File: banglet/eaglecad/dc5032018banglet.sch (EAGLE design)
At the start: 40 parts, among them Q3 DMG3415U-7, U2 AP2112(3.3V), U3 MCP73831T-2ACI/OT, U4 CP2104, X1 32.768, X2 JSTPH, X4 20329

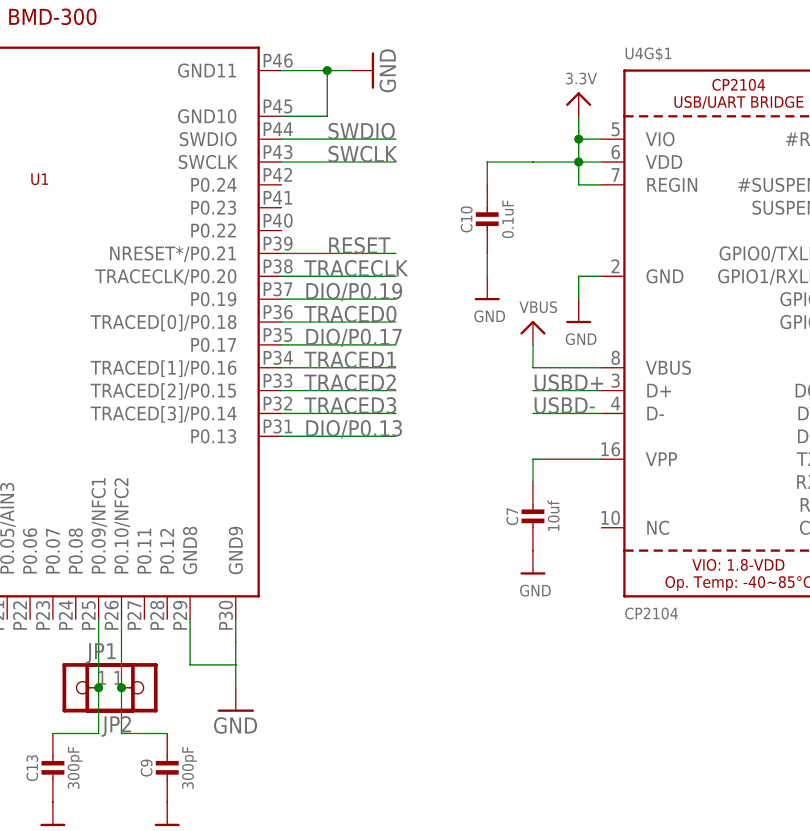
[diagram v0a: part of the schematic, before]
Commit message: Connect the unconnected; add in a junction
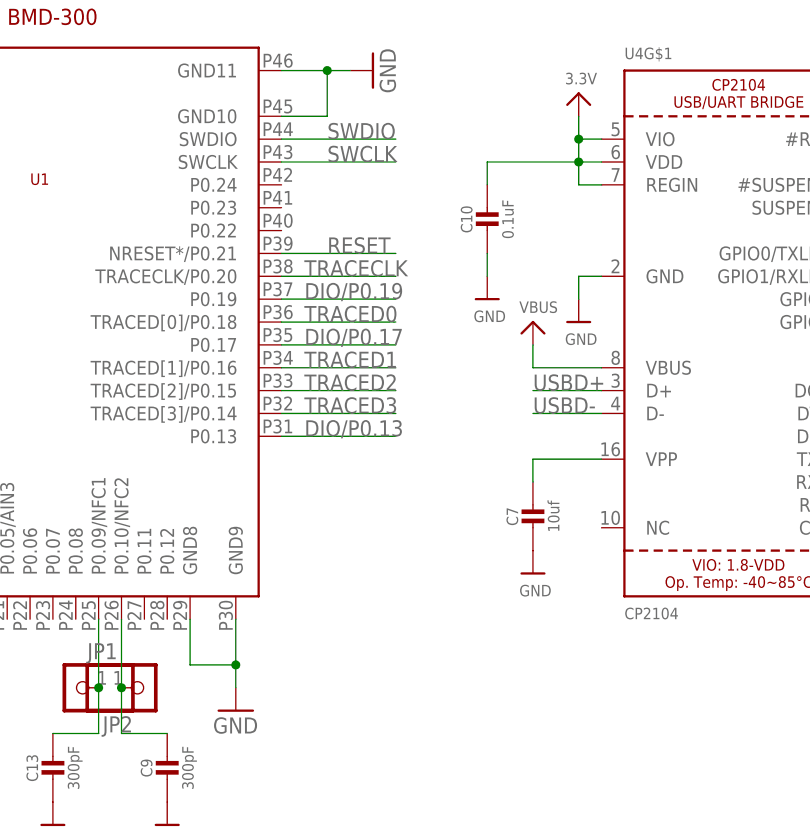
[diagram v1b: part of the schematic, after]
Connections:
- new net DIO/P0.17: U1.P0.17
- new net TRACED0: U1.TRACED[0]/P0.18
- new net TRACED1: U1.TRACED[1]/P0.16
- new net TRACED2: U1.TRACED[2]/P0.15
- new net TRACED3: U1.TRACED[3]/P0.14
- net RESET: now also U1.NRESET*/P0.21
- net SWCLK: now also U1.SWCLK
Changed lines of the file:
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@@
 <?xml version="1.0" encoding="utf-8"?>
 <!DOCTYPE eagle SYSTEM "eagle.dtd">
-<eagle version="8.2.1">
+<eagle version="8.6.3">
 <drawing>
 <settings>
 <setting alwaysvectorfont="no"/>
+<setting keepoldvectorfont="yes"/>
 <setting verticaltext="up"/>
 </settings>
@@
 <wire x1="22.86" y1="-43.18" x2="22.86" y2="-40.64" width="0.1524" layer="91"/>
 <pinref part="U1" gate="G$1" pin="GND8"/>
-<wire x1="22.86" y1="-38.1" x2="22.86" y2="-35.56" width="0.1524" layer="91"/>
 <wire x1="17.78" y1="-35.56" x2="17.78" y2="-40.64" width="0.1524" layer="91"/>
 <wire x1="17.78" y1="-40.64" x2="22.86" y2="-40.64" width="0.1524" layer="91"/>
-<wire x1="22.86" y1="-40.64" x2="22.86" y2="-38.1" width="0.1524" layer="91"/>
+<wire x1="22.86" y1="-40.64" x2="22.86" y2="-35.56" width="0.1524" layer="91"/>
+<junction x="22.86" y="-40.64"/>
 </segment>
 <segment>
@@
 <pinref part="C10" gate="G$1" pin="1"/>
 <wire x1="63.5" y1="15.24" x2="60.96" y2="15.24" width="0.1524" layer="91"/>
-<wire x1="60.96" y1="15.24" x2="55.88" y2="15.24" width="0.1524" layer="91"/>
-<wire x1="55.88" y1="15.24" x2="50.8" y2="15.24" width="0.1524" layer="91"/>
+<wire x1="60.96" y1="15.24" x2="50.8" y2="15.24" width="0.1524" layer="91"/>
 <wire x1="50.8" y1="15.24" x2="50.8" y2="12.7" width="0.1524" layer="91"/>
 <wire x1="60.96" y1="12.7" x2="60.96" y2="15.24" width="0.1524" layer="91"/>
@@
 <wire x1="27.94" y1="5.08" x2="40.64" y2="5.08" width="0.1524" layer="91"/>
 <label x="33.02" y="5.08" size="1.778" layer="95"/>
+<pinref part="U1" gate="G$1" pin="NRESET*/P0.21"/>
 </segment>
 </net>
@@
 <wire x1="27.94" y1="15.24" x2="40.64" y2="15.24" width="0.1524" layer="91"/>
 <label x="33.02" y="15.24" size="1.778" layer="95"/>
+<pinref part="U1" gate="G$1" pin="SWCLK"/>
 </segment>
 </net>
@@
 <wire x1="27.94" y1="-2.54" x2="40.64" y2="-2.54" width="0.1524" layer="91"/>
 <label x="30.48" y="-2.54" size="1.778" layer="95"/>
+<pinref part="U1" gate="G$1" pin="TRACED[0]/P0.18"/>
 </segment>
 </net>
@@
 <wire x1="27.94" y1="-12.7" x2="40.64" y2="-12.7" width="0.1524" layer="91"/>
 <label x="30.48" y="-12.7" size="1.778" layer="95"/>
+<pinref part="U1" gate="G$1" pin="TRACED[3]/P0.14"/>
 </segment>
 </net>
@@
 <wire x1="27.94" y1="-10.16" x2="40.64" y2="-10.16" width="0.1524" layer="91"/>
 <label x="30.48" y="-10.16" size="1.778" layer="95"/>
+<pinref part="U1" gate="G$1" pin="TRACED[2]/P0.15"/>
 </segment>
 </net>
@@
 <wire x1="27.94" y1="-7.62" x2="40.64" y2="-7.62" width="0.1524" layer="91"/>
 <label x="30.48" y="-7.62" size="1.778" layer="95"/>
+<pinref part="U1" gate="G$1" pin="TRACED[1]/P0.16"/>
 </segment>
 </net>
@@
 <wire x1="27.94" y1="-5.08" x2="40.64" y2="-5.08" width="0.1524" layer="91"/>
 <label x="30.48" y="-5.08" size="1.778" layer="95"/>
+<pinref part="U1" gate="G$1" pin="P0.17"/>
 </segment>
 </net>
@@
 </note>
 <note version="8.2" severity="warning">
-Since Version 8.2, Eagle supports online libraries. The ids
+Since Version 8.2, EAGLE supports online libraries. The ids
 of those online libraries will not be understood (or retained)
 with this version.

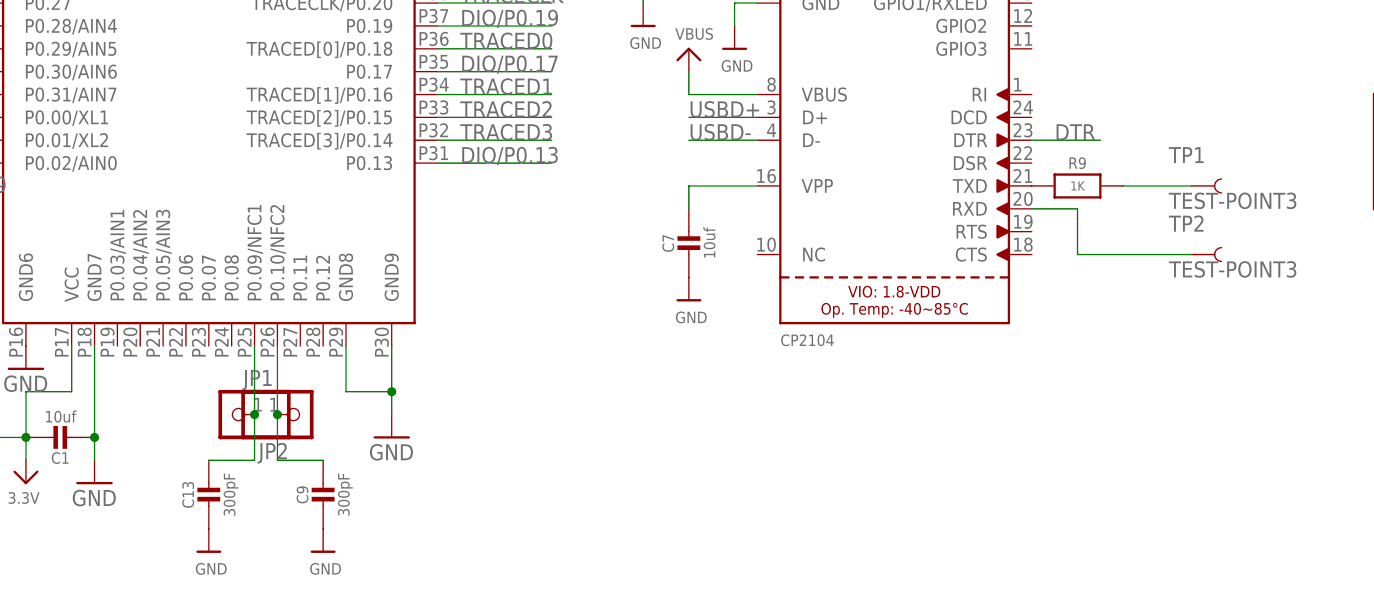
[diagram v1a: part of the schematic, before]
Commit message: connect uart tx/rx to bmd-300
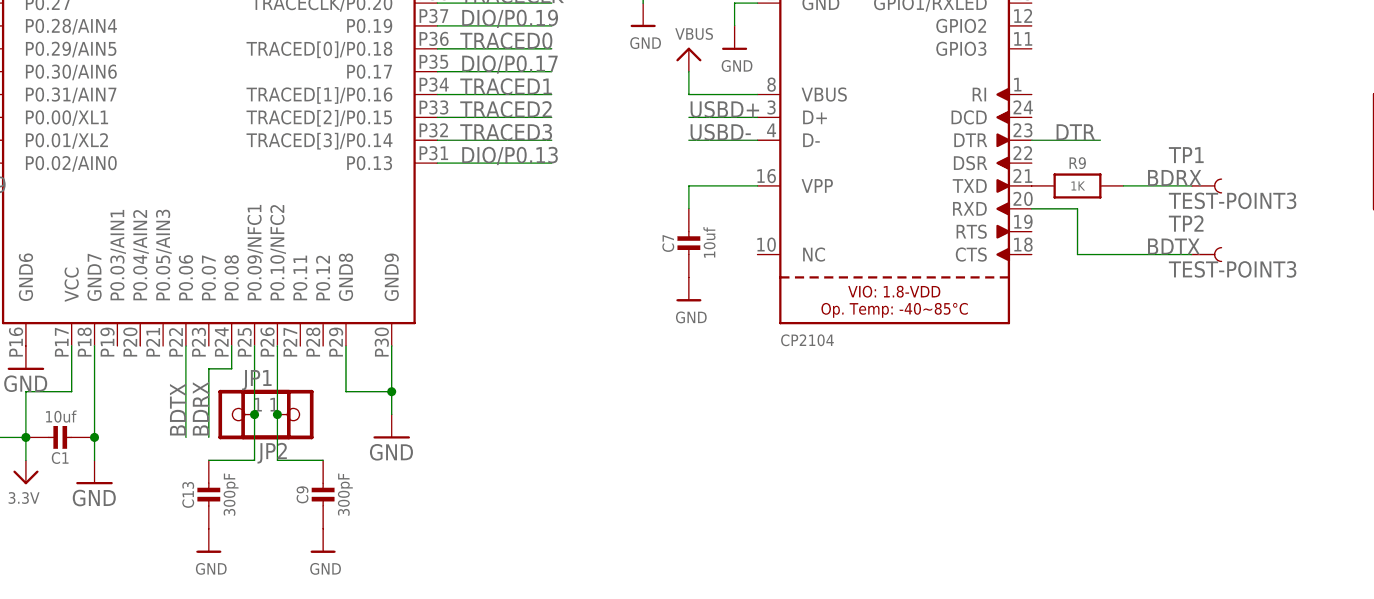
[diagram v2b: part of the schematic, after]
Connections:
- removed net N$3: R9.2, TP1.1
- removed net N$5: TP2.1, U4G$1.RXD
- new net BDRX: R9.2, TP1.1, U1.P0.08
- new net BDTX: TP2.1, U1.P0.06, U4G$1.RXD
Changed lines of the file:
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@@
 </segment>
 </net>
-<net name="VIN" class="0">
+<net name="VIN" class="1">
 <segment>
 <pinref part="D5" gate="G$1" pin="C"/>
@@
 </segment>
 </net>
-<net name="N$3" class="0">
-<segment>
-<pinref part="R9" gate="G$1" pin="2"/>
-<wire x1="111.76" y1="-17.78" x2="104.14" y2="-17.78" width="0.1524" layer="91"/>
-<pinref part="TP1" gate="G$1" pin="1"/>
-</segment>
-</net>
-<net name="N$5" class="0">
-<segment>
-<pinref part="U4" gate="G$1" pin="RXD"/>
-<wire x1="93.98" y1="-20.32" x2="99.06" y2="-20.32" width="0.1524" layer="91"/>
-<wire x1="99.06" y1="-20.32" x2="99.06" y2="-25.4" width="0.1524" layer="91"/>
-<wire x1="99.06" y1="-25.4" x2="111.76" y2="-25.4" width="0.1524" layer="91"/>
-<pinref part="TP2" gate="G$1" pin="1"/>
-</segment>
-</net>
 <net name="N$6" class="0">
 <segment>
@@
 </segment>
 </net>
+<net name="BDRX" class="0">
+<segment>
+<pinref part="U1" gate="G$1" pin="P0.08"/>
+<wire x1="5.08" y1="-35.56" x2="5.08" y2="-38.1" width="0.1524" layer="91"/>
+<wire x1="5.08" y1="-38.1" x2="2.54" y2="-38.1" width="0.1524" layer="91"/>
+<wire x1="2.54" y1="-38.1" x2="2.54" y2="-45.72" width="0.1524" layer="91"/>
+<label x="2.54" y="-45.72" size="1.778" layer="95" rot="R90"/>
+</segment>
+<segment>
+<pinref part="R9" gate="G$1" pin="2"/>
+<wire x1="111.76" y1="-17.78" x2="104.14" y2="-17.78" width="0.1524" layer="91"/>
+<pinref part="TP1" gate="G$1" pin="1"/>
+<label x="106.68" y="-17.78" size="1.778" layer="95"/>
+</segment>
+</net>
+<net name="BDTX" class="0">
+<segment>
+<pinref part="U1" gate="G$1" pin="P0.06"/>
+<wire x1="0" y1="-35.56" x2="0" y2="-45.72" width="0.1524" layer="91"/>
+<label x="0" y="-45.72" size="1.778" layer="95" rot="R90"/>
+</segment>
+<segment>
+<pinref part="U4" gate="G$1" pin="RXD"/>
+<wire x1="93.98" y1="-20.32" x2="99.06" y2="-20.32" width="0.1524" layer="91"/>
+<wire x1="99.06" y1="-20.32" x2="99.06" y2="-25.4" width="0.1524" layer="91"/>
+<wire x1="99.06" y1="-25.4" x2="111.76" y2="-25.4" width="0.1524" layer="91"/>
+<pinref part="TP2" gate="G$1" pin="1"/>
+<label x="106.68" y="-25.4" size="1.778" layer="95"/>
+</segment>
+</net>

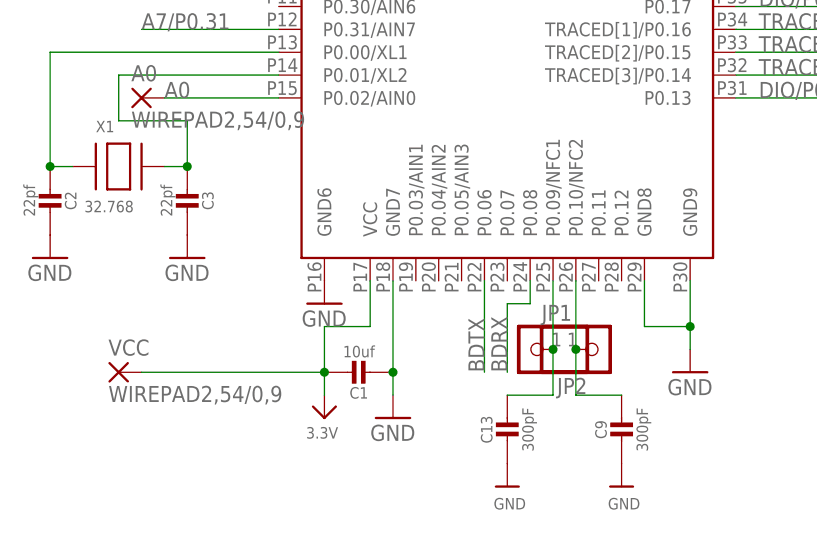
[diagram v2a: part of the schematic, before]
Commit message: changed layout to perhaps better/easier routing.  Routed.
Opinions saught.
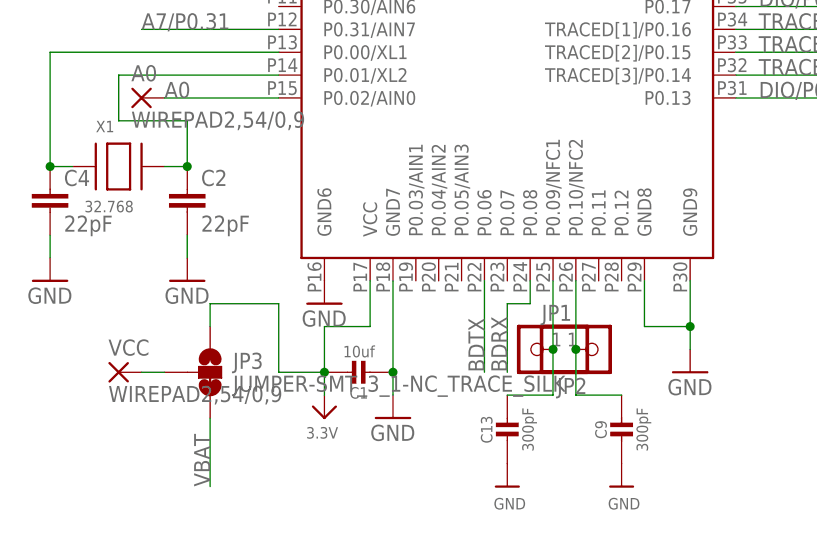
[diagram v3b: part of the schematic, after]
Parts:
- removed C3: 22pf, microbuilder:CAP_CERAMIC0805-NOOUTLINE
- added C4: 22pF, SparkFun-Capacitors:22PF-0603-50V-5%
- added JP3: JUMPER-SMT_3_1-NC_TRACE_SILK, SparkFun-Jumpers:JUMPER-SMT_3_1-NC_TRACE_SILK
- C2: value 22pf -> 22pF; device microbuilder:CAP_CERAMIC0805-NOOUTLINE -> SparkFun-Capacitors:22PF-0603-50V-5%
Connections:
- new net N$3: JP3.2, VCC.P
- net 3.3V: now also JP3.1; no longer VCC.P
- net GND: now also C2.2, C4.2; no longer C2.1, C3.1
- net N$1: now also C2.1; no longer C3.2
- net N$2: now also C4.1; no longer C2.2
- net VBAT: now also JP3.3
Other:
- moved on the sheet: C2
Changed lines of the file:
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@@
 <part name="U$1" library="microbuilder" deviceset="3.3V" device=""/>
 <part name="C1" library="microbuilder" deviceset="CAP_CERAMIC" device="0805-NOOUTLINE" value="10uf"/>
-<part name="C2" library="microbuilder" deviceset="CAP_CERAMIC" device="0805-NOOUTLINE" value="22pf"/>
-<part name="C3" library="microbuilder" deviceset="CAP_CERAMIC" device="0805-NOOUTLINE" value="22pf"/>
 <part name="GND7" library="supply1" library_urn="urn:adsk.eagle:library:371" deviceset="GND" device=""/>
 <part name="GND8" library="supply1" library_urn="urn:adsk.eagle:library:371" deviceset="GND" device=""/>
@@
 <part name="TP1" library="SparkFun-Connectors" library_urn="urn:adsk.eagle:library:513" deviceset="TEST-POINT" device="3"/>
 <part name="TP2" library="SparkFun-Connectors" library_urn="urn:adsk.eagle:library:513" deviceset="TEST-POINT" device="3"/>
+<part name="JP3" library="SparkFun-Jumpers" library_urn="urn:adsk.eagle:library:528" deviceset="JUMPER-SMT_3_1-NC_TRACE" device="_SILK" package3d_urn="urn:adsk.eagle:package:39288/1"/>
+<part name="C4" library="SparkFun-Capacitors" library_urn="urn:adsk.eagle:library:510" deviceset="22PF" device="-0603-50V-5%" package3d_urn="urn:adsk.eagle:package:37414/1" value="22pF"/>
+<part name="C2" library="SparkFun-Capacitors" library_urn="urn:adsk.eagle:library:510" deviceset="22PF" device="-0603-50V-5%" package3d_urn="urn:adsk.eagle:package:37414/1" value="22pF"/>
 </parts>
 <sheets>
@@
 <instance part="U$1" gate="G$1" x="-17.78" y="-50.8" rot="R180"/>
 <instance part="C1" gate="G$1" x="-12.7" y="-45.72" rot="R90"/>
-<instance part="C2" gate="G$1" x="-48.26" y="-25.4" rot="R180"/>
-<instance part="C3" gate="G$1" x="-33.02" y="-25.4" rot="R180"/>
-<instance part="GND7" gate="1" x="-48.26" y="-33.02"/>
-<instance part="GND8" gate="1" x="-33.02" y="-33.02"/>
+<instance part="GND7" gate="1" x="-48.26" y="-35.56"/>
+<instance part="GND8" gate="1" x="-33.02" y="-35.56"/>
 <instance part="X1" gate="G$1" x="-40.64" y="-22.86"/>
 <instance part="JP1" gate="G$1" x="12.7" y="-43.18"/>
@@
 <instance part="TP1" gate="G$1" x="111.76" y="-17.78"/>
 <instance part="TP2" gate="G$1" x="111.76" y="-25.4"/>
+<instance part="JP3" gate="G$1" x="-30.48" y="-45.72"/>
+<instance part="C4" gate="G$1" x="-48.26" y="-27.94"/>
+<instance part="C2" gate="G$1" x="-33.02" y="-27.94"/>
 </instances>
 <busses>
@@
 <wire x1="-10.16" y1="-45.72" x2="-10.16" y2="-35.56" width="0.1524" layer="91"/>
 <junction x="-10.16" y="-45.72"/>
-</segment>
-<segment>
-<pinref part="C2" gate="G$1" pin="1"/>
-<pinref part="GND7" gate="1" pin="GND"/>
-</segment>
-<segment>
-<pinref part="C3" gate="G$1" pin="1"/>
-<pinref part="GND8" gate="1" pin="GND"/>
 </segment>
 <segment>
@@
 <pinref part="U$11" gate="G$1" pin="GND"/>
 </segment>
+<segment>
+<pinref part="GND7" gate="1" pin="GND"/>
+<pinref part="C4" gate="G$1" pin="2"/>
+<wire x1="-48.26" y1="-33.02" x2="-48.26" y2="-30.48" width="0.1524" layer="91"/>
+</segment>
+<segment>
+<pinref part="GND8" gate="1" pin="GND"/>
+<pinref part="C2" gate="G$1" pin="2"/>
+<wire x1="-33.02" y1="-33.02" x2="-33.02" y2="-30.48" width="0.1524" layer="91"/>
+</segment>
 </net>
 <net name="3.3V" class="1">
@@
 <wire x1="-17.78" y1="-45.72" x2="-17.78" y2="-48.26" width="0.1524" layer="91"/>
 <junction x="-17.78" y="-45.72"/>
-<pinref part="VCC" gate="G$1" pin="P"/>
-<wire x1="-38.1" y1="-45.72" x2="-17.78" y2="-45.72" width="0.1524" layer="91"/>
+<pinref part="JP3" gate="G$1" pin="1"/>
+<wire x1="-30.48" y1="-40.64" x2="-30.48" y2="-38.1" width="0.1524" layer="91"/>
+<wire x1="-30.48" y1="-38.1" x2="-22.86" y2="-38.1" width="0.1524" layer="91"/>
+<wire x1="-22.86" y1="-38.1" x2="-22.86" y2="-45.72" width="0.1524" layer="91"/>
+<wire x1="-22.86" y1="-45.72" x2="-17.78" y2="-45.72" width="0.1524" layer="91"/>
 </segment>
 <segment>
@@
 <pinref part="R4" gate="G$1" pin="1"/>
 <pinref part="U$14" gate="G$1" pin="VBAT"/>
+</segment>
+<segment>
+<pinref part="JP3" gate="G$1" pin="3"/>
+<wire x1="-30.48" y1="-50.8" x2="-30.48" y2="-58.42" width="0.1524" layer="91"/>
+<label x="-30.48" y="-58.42" size="1.778" layer="95" rot="R90"/>
 </segment>
 </net>
@@
 </segment>
 </net>
-<net name="N$14" class="0">
+<net name="N$14" class="1">
 <segment>
 <pinref part="U4" gate="G$1" pin="VPP"/>
@@
 <segment>
 <pinref part="X1" gate="G$1" pin="P$2"/>
-<pinref part="C3" gate="G$1" pin="2"/>
 <wire x1="-33.02" y1="-22.86" x2="-33.02" y2="-17.78" width="0.1524" layer="91"/>
-<junction x="-33.02" y="-22.86"/>
 <wire x1="-33.02" y1="-17.78" x2="-40.64" y2="-17.78" width="0.1524" layer="91"/>
 <wire x1="-40.64" y1="-17.78" x2="-40.64" y2="-12.7" width="0.1524" layer="91"/>
@@
 <wire x1="-40.64" y1="-12.7" x2="-22.86" y2="-12.7" width="0.1524" layer="91"/>
 <wire x1="-33.02" y1="-22.86" x2="-35.56" y2="-22.86" width="0.1524" layer="91"/>
+<pinref part="C2" gate="G$1" pin="1"/>
+<junction x="-33.02" y="-22.86"/>
 </segment>
 </net>
@@
 <segment>
 <pinref part="X1" gate="G$1" pin="P$1"/>
-<pinref part="C2" gate="G$1" pin="2"/>
 <wire x1="-48.26" y1="-22.86" x2="-48.26" y2="-10.16" width="0.1524" layer="91"/>
-<junction x="-48.26" y="-22.86"/>
 <pinref part="U1" gate="G$1" pin="P0.00/XL1"/>
 <wire x1="-48.26" y1="-10.16" x2="-22.86" y2="-10.16" width="0.1524" layer="91"/>
 <wire x1="-48.26" y1="-22.86" x2="-45.72" y2="-22.86" width="0.1524" layer="91"/>
+<pinref part="C4" gate="G$1" pin="1"/>
+<junction x="-48.26" y="-22.86"/>
 </segment>
 </net>
@@
 <pinref part="TP2" gate="G$1" pin="1"/>
 <label x="106.68" y="-25.4" size="1.778" layer="95"/>
+</segment>
+</net>
+<net name="N$3" class="0">
+<segment>
+<pinref part="VCC" gate="G$1" pin="P"/>
+<pinref part="JP3" gate="G$1" pin="2"/>
+<wire x1="-38.1" y1="-45.72" x2="-35.56" y2="-45.72" width="0.1524" layer="91"/>
 </segment>
 </net>
@@
 with this version.
 </note>
+<note version="8.3" severity="warning">
+Since Version 8.3, EAGLE supports URNs for individual library
+assets (packages, symbols, and devices). The URNs of those assets
+will not be understood (or retained) with this version.
+</note>
+<note version="8.3" severity="warning">
+Since Version 8.3, EAGLE supports the association of 3D packages
+with devices in libraries, schematics, and board files. Those 3D
+packages will not be understood (or retained) with this version.
+</note>
 </compatibility>
